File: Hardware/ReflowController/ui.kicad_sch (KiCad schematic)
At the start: 0 parts

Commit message: Finished the fan controllers calculations, added the wago connectors, added notes
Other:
- title: (none) -> Reflow Oven Control
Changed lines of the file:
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@@
 (kicad_sch (version 20230121) (generator eeschema)
   (paper "A4")
+  (title_block
+    (title "Reflow Oven Control")
+    (rev "0.1")
+  )
   (text "IO expander PI4IOE5V6416LEX" (at 133.35 102.87 0)
     (effects (font (size 1.27 1.27)) (justify left bottom))

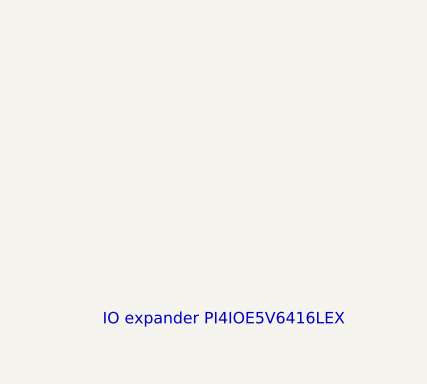
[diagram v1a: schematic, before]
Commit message: Added the IO expander and RJ45 Connectors for LCD and Keypad Connectors
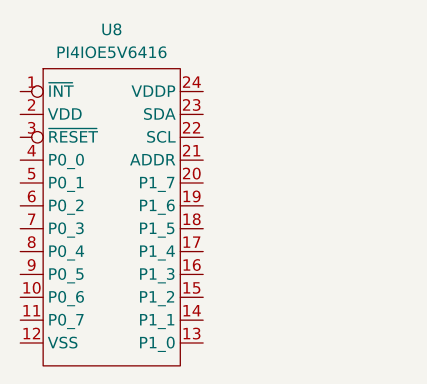
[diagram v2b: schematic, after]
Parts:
- added U8: PI4IOE5V6416, Package_SO:TSSOP-24_4.4x7.8mm_P0.65mm, symbol 470_digital_io_port_expander:PI4IOE5V6416
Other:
- note removed: "IO expander PI4IOE5V6416LEX"
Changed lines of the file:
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@@
     (rev "0.1")
   )
-  (text "IO expander PI4IOE5V6416LEX" (at 133.35 102.87 0)
-    (effects (font (size 1.27 1.27)) (justify left bottom))
+  (symbol (lib_id "470_digital_io_port_expander:PI4IOE5V6416") (at 134.366 89.408 0) (unit 1)
+    (in_bom yes) (on_board yes) (dnp no) (fields_autoplaced)
+    (property "Reference" "U8" (at 134.366 69.85 0)
+      (effects (font (size 1.27 1.27)))
+    )
+    (property "Value" "PI4IOE5V6416" (at 134.366 72.39 0)
+      (effects (font (size 1.27 1.27)))
+    )
+    (property "Footprint" "Package_SO:TSSOP-24_4.4x7.8mm_P0.65mm" (at 155.956 37.338 0)
+      (effects (font (size 1.27 1.27)) hide)
+    )
+    (property "Datasheet" "https://www.diodes.com/assets/Datasheets/PI4IOE5V6416.pdf" (at 164.846 39.878 0)
+      (effects (font (size 1.27 1.27)) hide)
+    )
+    (property "man" "diodes" (at 129.286 34.798 0)
+      (effects (font (size 1.27 1.27)) hide)
+    )
+    (property "man_no" "PI4IOE5V6416LEX" (at 143.256 34.798 0)
+      (effects (font (size 1.27 1.27)) hide)
+    )
+    (property "disti" "digikey" (at 129.286 42.418 0)
+      (effects (font (size 1.27 1.27)) hide)
+    )
+    (property "disti_no" "PI4IOE5V6416LEXDITR-ND" (at 147.066 42.418 0)
+      (effects (font (size 1.27 1.27)) hide)
+    )
+    (pin "1")
+    (pin "10")
+    (pin "11")
+    (pin "12")
+    (pin "13")
+    (pin "14")
+    (pin "15")
+    (pin "16")
+    (pin "17")
+    (pin "18")
+    (pin "19")
+    (pin "2")
+    (pin "20")
+    (pin "21")
+    (pin "22")
+    (pin "23")
+    (pin "24")
+    (pin "3")
+    (pin "4")
+    (pin "5")
+    (pin "6")
+    (pin "7")
+    (pin "8")
+    (pin "9")
+    (instances
+      (project "ReflowController"
+        (path "/2394cc2a-b9b0-4c0b-be11-1fc6085b0d5c/c76c60d6-41ab-4683-93d6-43449ec74daf"
+          (reference "U8") (unit 1)
+        )
+      )
+    )
   )
 )

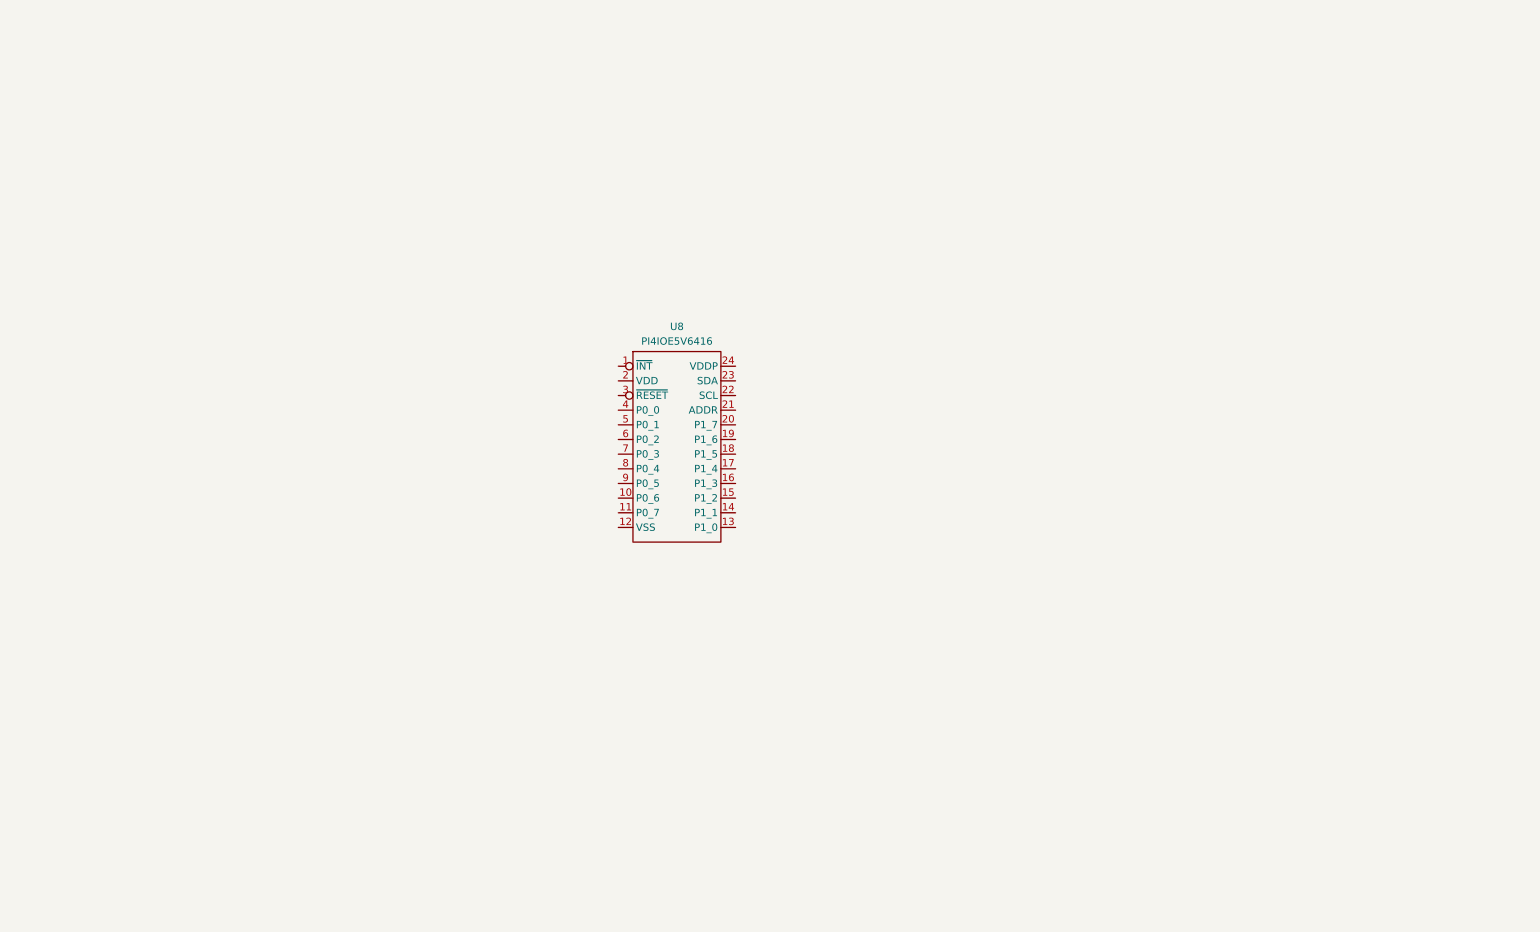
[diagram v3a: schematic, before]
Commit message: finished the io control for the pcb, need to define what is the best way for a remote keypad
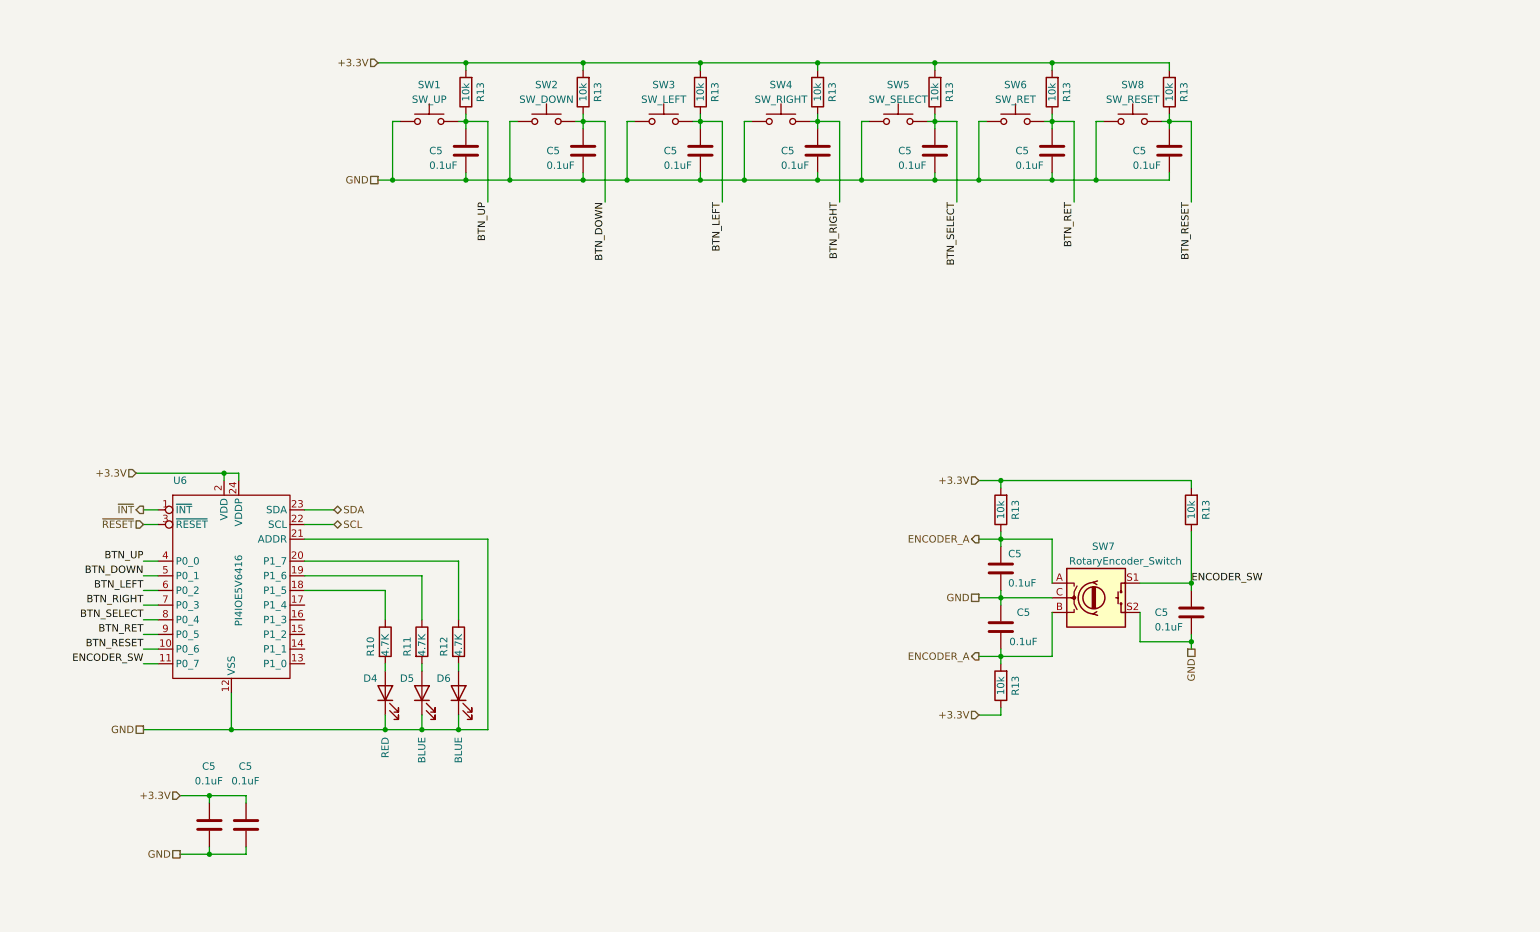
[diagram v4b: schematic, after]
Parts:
- added C5 (x12): 0.1uF, Capacitor_SMD:C_0603_1608Metric_Pad1.08x0.95mm_HandSolder, symbol Device:C
- added D4: RED, LED_SMD:LED_0603_1608Metric_Pad1.05x0.95mm_HandSolder, symbol Device:LED
- added D5, D6: BLUE, LED_SMD:LED_0603_1608Metric_Pad1.05x0.95mm_HandSolder, symbol Device:LED
- added R10, R11, R12: 4.7K, Resistor_SMD:R_0603_1608Metric_Pad0.98x0.95mm_HandSolder, symbol Device:R
- added R13 (x10): 10k, Resistor_SMD:R_0603_1608Metric_Pad0.98x0.95mm_HandSolder, symbol Device:R
- added SW1: SW_UP, Button_Switch_SMD:SW_SPST_B3S-1000, symbol Switch:SW_Push
- added SW2: SW_DOWN, Button_Switch_SMD:SW_SPST_B3S-1000, symbol Switch:SW_Push
- added SW3: SW_LEFT, Button_Switch_SMD:SW_SPST_B3S-1000, symbol Switch:SW_Push
- added SW4: SW_RIGHT, Button_Switch_SMD:SW_SPST_B3S-1000, symbol Switch:SW_Push
- added SW5: SW_SELECT, Button_Switch_SMD:SW_SPST_B3S-1000, symbol Switch:SW_Push
- added SW6: SW_RET, Button_Switch_SMD:SW_SPST_B3S-1000, symbol Switch:SW_Push
- added SW7: RotaryEncoder_Switch, Rotary_Encoder:RotaryEncoder_Alps_EC11E-Switch_Vertical_H20mm, symbol Device:RotaryEncoder_Switch
- added SW8: SW_RESET, Button_Switch_SMD:SW_SPST_B3S-1000, symbol Switch:SW_Push
- renumbered U8 to U6
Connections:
- net ~{INT}: now reaches U6.1 (~{INT})
- net BTN_RESET: now reaches U6.10 (P0_6)
- net BTN_RESET: now also C5.1, R13.1, SW8.2
- net ENCODER_SW: now reaches U6.11 (P0_7)
- net ENCODER_SW: now also C5.1, R13.1, SW7.S1
- net GND: now reaches U6.12 (VSS)
- net GND: now also U6.21 (ADDR), C5.2, C5.2, C5.2, C5.2, C5.2, C5.2, C5.2, C5.2, C5.2, C5.2, C5.2, C5.2, D4.1 (K), D5.1 (K), D6.1 (K), SW1.1, SW2.1, SW3.1, SW4.1, SW5.1, SW6.1, SW7.C, SW7.S2, SW8.1
- net at U6.18 (P1_5): now also R10.1
- net at U6.19 (P1_6): now also R11.1
- net +3.3V: now reaches U6.2 (VDD)
- net +3.3V: now also U6.24 (VDDP), C5.1, C5.1, R13.1, R13.2, R13.2, R13.2, R13.2, R13.2, R13.2, R13.2, R13.2, R13.2
- net at U6.20 (P1_7): now also R12.1
- net SCL: now reaches U6.22 (SCL)
- net SDA: now reaches U6.23 (SDA)
- net ~{RESET}: now reaches U6.3 (~{RESET})
- net BTN_UP: now reaches U6.4 (P0_0)
- net BTN_UP: now also C5.1, R13.1, SW1.2
- net BTN_DOWN: now reaches U6.5 (P0_1)
- net BTN_DOWN: now also C5.1, R13.1, SW2.2
- net BTN_LEFT: now reaches U6.6 (P0_2)
- net BTN_LEFT: now also C5.1, R13.1, SW3.2
- net BTN_RIGHT: now reaches U6.7 (P0_3)
- net BTN_RIGHT: now also C5.1, R13.1, SW4.2
- net BTN_SELECT: now reaches U6.8 (P0_4)
- net BTN_SELECT: now also C5.1, R13.1, SW5.2
- net BTN_RET: now reaches U6.9 (P0_5)
- net BTN_RET: now also C5.1, R13.1, SW6.2
- new net: D6.2 (A), R12.2
- new net: D5.2 (A), R11.2
- new net: D4.2 (A), R10.2
- new net ENCODER_A: C5.1, C5.1, R13.1, R13.2, SW7.A, SW7.B
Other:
- moved on the sheet: U6

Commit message: Wrking with edwin on the hwole schematic
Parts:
- added BZ1: Buzzer, Buzzer_Beeper:Buzzer_TDK_PS1240P02BT_D12.2mm_H6.5mm, symbol Device:Buzzer
- added C5: 0.1uF, Capacitor_SMD:C_0603_1608Metric_Pad1.08x0.95mm_HandSolder, symbol Device:C
- added J15: LCD_HEADER, Connector_PinSocket_2.54mm:PinSocket_1x07_P2.54mm_Vertical, symbol Connector:Conn_01x07_Female
- added Q2: BC848, Package_TO_SOT_SMD:SOT-23, symbol Transistor_BJT:BC848
- added R13: 10k, Resistor_SMD:R_0603_1608Metric_Pad0.98x0.95mm_HandSolder, symbol Device:R
- added R38, R39: 1k, Resistor_SMD:R_1206_3216Metric_Pad1.42x1.75mm_HandSolder, symbol Device:R
- added TP1: IO_AUX_1, TestPoint:TestPoint_Pad_D1.5mm, symbol Connector:TestPoint
- added TP2: IO_AUX_2, TestPoint:TestPoint_Pad_D1.5mm, symbol Connector:TestPoint
- D5: value BLUE -> GREEN; disti_no 160-1827-2-ND -> 160-1446-2-ND; man_no LTST-C193TBKT-5A -> LTST-C191KGKT
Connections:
- net ENCODER_A: now also U6.13 (P1_0); no longer C5.1, R13.2, SW7.B
- net ENCODER_SW: now also U6.15 (P1_2)
- net SCL: now also J15.3 (Pin_3)
- net SDA: now also J15.4 (Pin_4)
- net ~{RESET}: now also J15.5 (Pin_5)
- net IO_AUX_2: now reaches U6.20 (P1_7)
- net IO_AUX_2: now also TP2.1; no longer R12.1
- net IO_AUX_1: now reaches U6.19 (P1_6)
- net IO_AUX_1: now also TP1.1; no longer R11.1
- net LED_ERROR: now reaches R10.1
- net LED_ERROR: now also U6.16 (P1_3); no longer U6.18 (P1_5)
- net ENCODER_B: now reaches U6.14 (P1_1)
- net ENCODER_B: now also C5.1, R13.2, SW7.B
- net LED_ALIVE: now reaches U6.17 (P1_4)
- net LED_ALIVE: now also R11.1
- net +3.3V renamed +3.3VD
- net +3.3VD: now also BZ1.1 (-), C5.1, J15.2 (Pin_2), R39.1
- net GND renamed DGND
- net DGND: now also C5.2, J15.1 (Pin_1), J15.6 (Pin_6), J15.7 (Pin_7), Q2.2 (E), R13.1
- new net: BZ1.2 (+), Q2.3 (C), R39.2
- new net: Q2.1 (B), R13.2, R38.1
- new net BUZZER_PWM: R38.2
- new net LED_INDICATION: R12.1, U6.18 (P1_5)
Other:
- note added: "BUTTONS"
- note added: "BUZZER"
- note added: "Docks to 0.96 inch OLED display"
- note added: "ENCODER"
- note added: "IO EXPNADER AND LEDS"
- note added: "LCD HEADER"
- moved on the sheet: C5, D4, D5, D6, R10, R11, R12, R13, SW1, SW2, SW3, SW4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

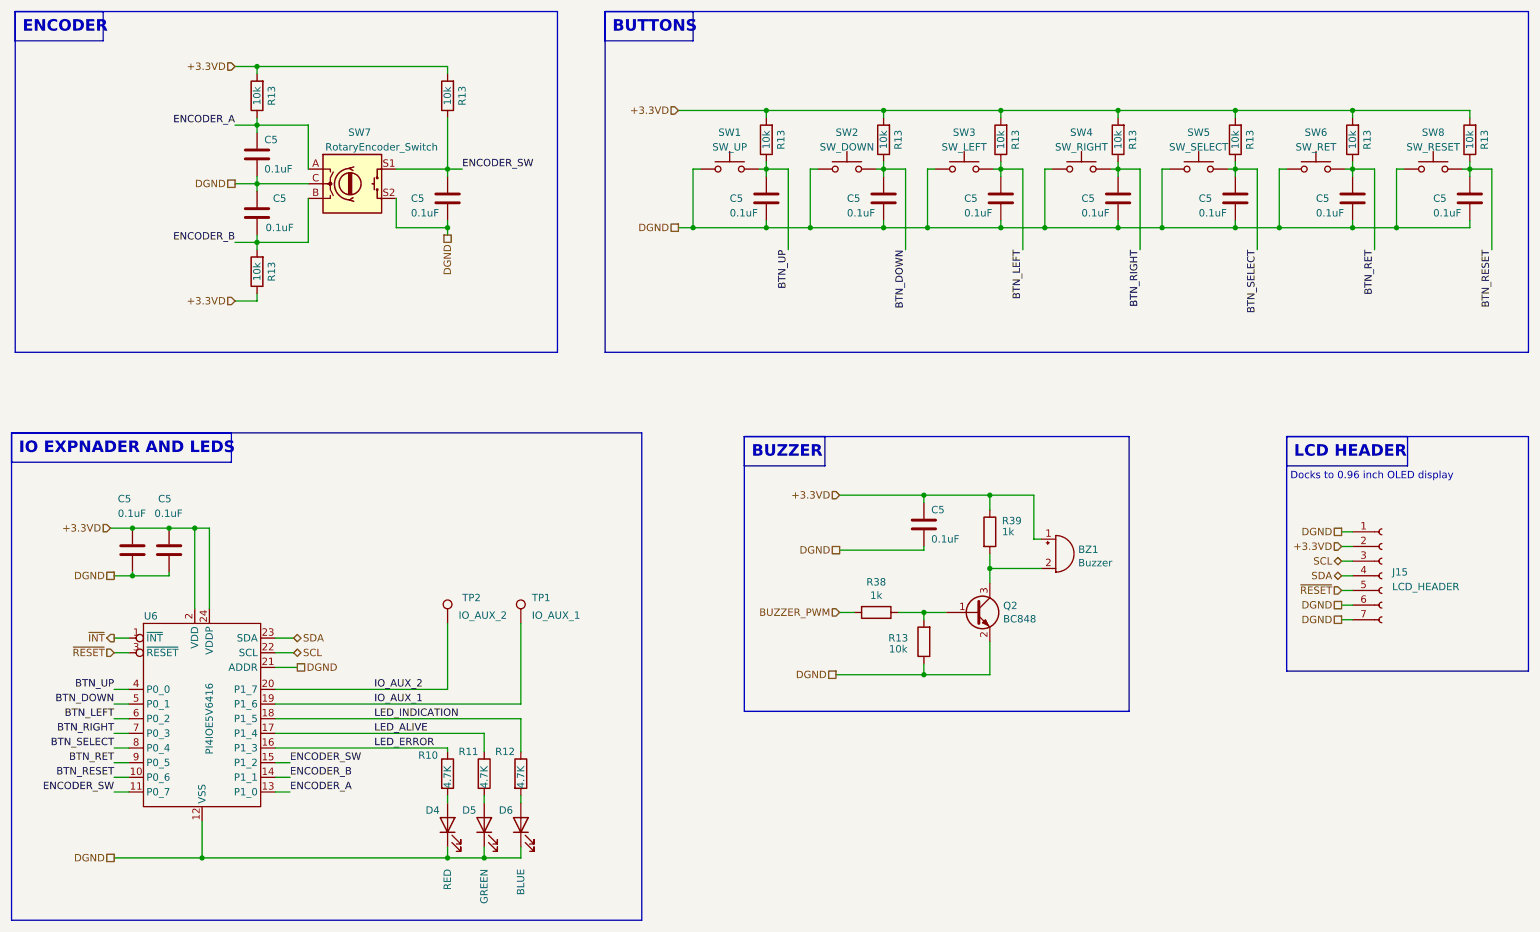
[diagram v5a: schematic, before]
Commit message: Finished the desing of the PSUand started with the PCB TODO: missing fuse find a solution
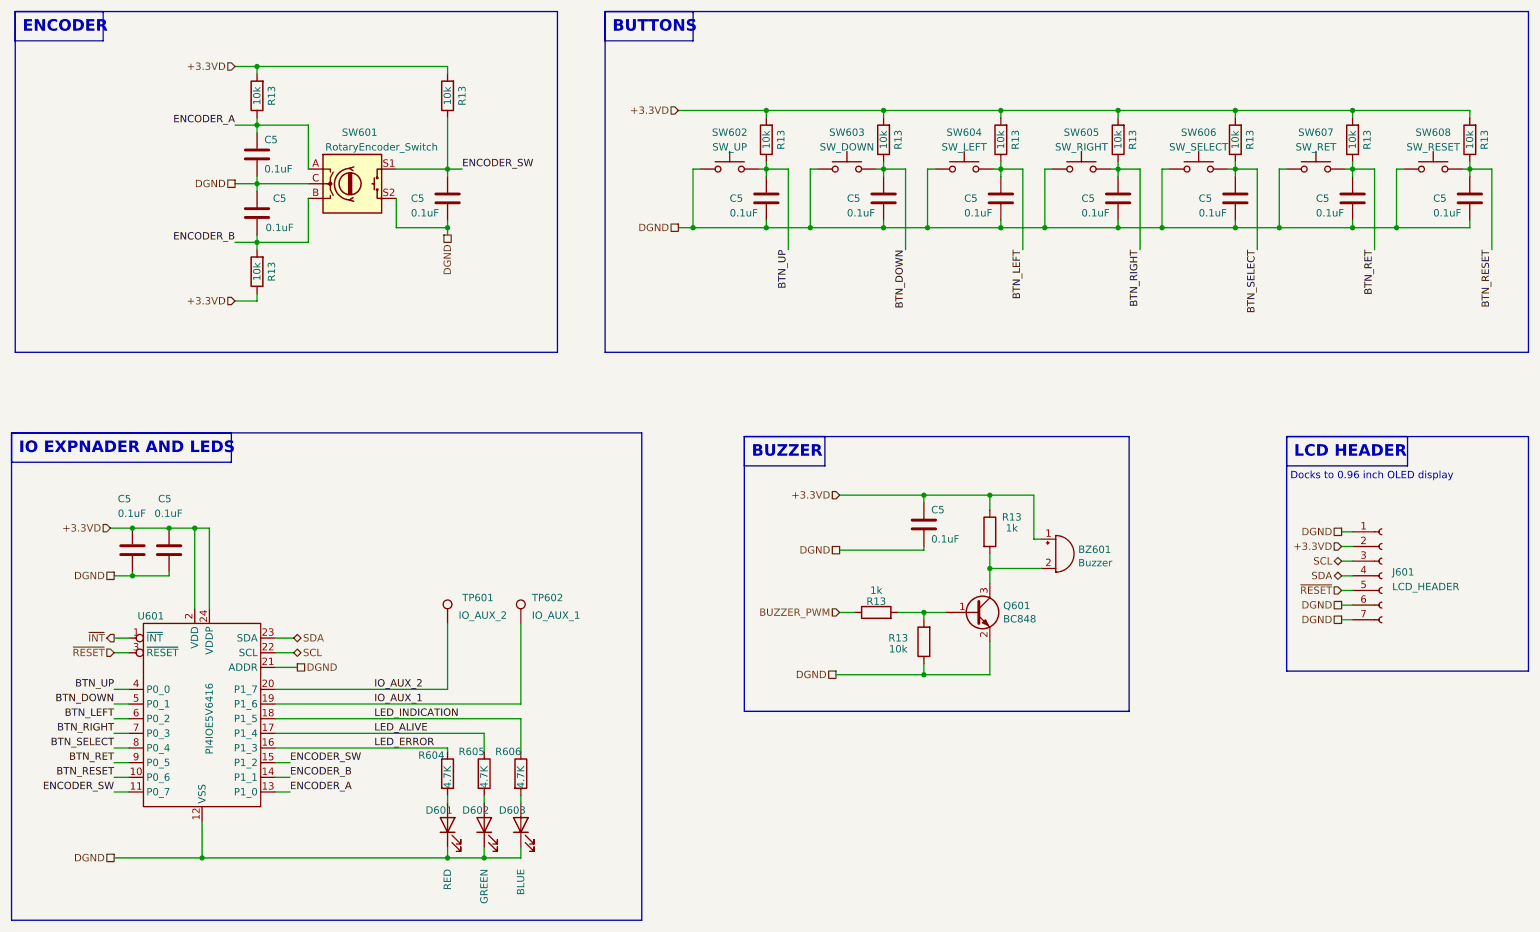
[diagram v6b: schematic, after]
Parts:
- removed R38, R39: 1k, Resistor_SMD:R_1206_3216Metric_Pad1.42x1.75mm_HandSolder, symbol Device:R
- added R13 (x2): 1k, Resistor_SMD:R_0603_1608Metric_Pad0.98x0.95mm_HandSolder, symbol Device:R
- renumbered BZ1 to BZ601, D4 to D601, D5 to D602, D6 to D603, J15 to J601, Q2 to Q601, R10 to R604, R11 to R605, R12 to R606, SW7 to SW601, SW1 to SW602, SW2 to SW603, SW3 to SW604, SW4 to SW605, SW5 to SW606, SW6 to SW607, SW8 to SW608, TP2 to TP601, TP1 to TP602, U6 to U601
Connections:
- net +3.3VD: now also R13.1
- net BUZZER_PWM: now also R13.1
- net at BZ601.2 (+), Q601.3 (C): now also R13.2
- net at Q601.1 (B), R13.2: now also R13.2

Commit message: Made some progress on the PCB desgin for now only the main blocks are complete, thw pin connection of the mCU should be organised and Net-ties are making life much harder as you cant put them on the middle layers
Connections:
- net BTN_DOWN: now also U601.6 (P0_2); no longer U601.5 (P0_1)
- net BTN_LEFT: now also U601.7 (P0_3); no longer U601.6 (P0_2)
- net BTN_RESET: now also U601.5 (P0_1); no longer U601.10 (P0_6)
- net BTN_RET: now also U601.4 (P0_0); no longer U601.9 (P0_5)
- net BTN_RIGHT: now also U601.10 (P0_6); no longer U601.7 (P0_3)
- net BTN_UP: now also U601.9 (P0_5); no longer U601.4 (P0_0)
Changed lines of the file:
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@@
     (effects (font (size 1.27 1.27)) (justify right bottom))
   )
-  (label "BTN_RIGHT" (at 36.83 140.335 180) (fields_autoplaced)
+  (label "BTN_RIGHT" (at 36.83 147.955 180) (fields_autoplaced)
     (effects (font (size 1.27 1.27)) (justify right bottom))
   )
@@
     (effects (font (size 1.27 1.27)) (justify left bottom))
   )
-  (label "BTN_RESET" (at 36.83 147.955 180) (fields_autoplaced)
+  (label "BTN_RESET" (at 36.83 135.255 180) (fields_autoplaced)
     (effects (font (size 1.27 1.27)) (justify right bottom))
   )
@@
     (effects (font (size 1.27 1.27)) (justify right bottom))
   )
-  (label "BTN_UP" (at 36.83 132.715 180) (fields_autoplaced)
+  (label "BTN_UP" (at 36.83 145.415 180) (fields_autoplaced)
     (effects (font (size 1.27 1.27)) (justify right bottom))
   )
@@
     (effects (font (size 1.27 1.27)) (justify right bottom))
   )
-  (label "BTN_LEFT" (at 36.83 137.795 180) (fields_autoplaced)
+  (label "BTN_LEFT" (at 36.83 140.335 180) (fields_autoplaced)
     (effects (font (size 1.27 1.27)) (justify right bottom))
   )
@@
     (effects (font (size 1.27 1.27)) (justify right bottom))
   )
-  (label "BTN_RET" (at 36.83 145.415 180) (fields_autoplaced)
+  (label "BTN_RET" (at 36.83 132.715 180) (fields_autoplaced)
     (effects (font (size 1.27 1.27)) (justify right bottom))
   )
@@
     (effects (font (size 1.27 1.27)) (justify left bottom))
   )
-  (label "BTN_DOWN" (at 36.83 135.255 180) (fields_autoplaced)
+  (label "BTN_DOWN" (at 36.83 137.795 180) (fields_autoplaced)
     (effects (font (size 1.27 1.27)) (justify right bottom))
   )
